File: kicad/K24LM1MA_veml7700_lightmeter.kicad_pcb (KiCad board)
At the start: 2 copper layers, 38.7 x 43.9 mm, 47 parts, among them J1 Conn_01x08_Socket, J2 Conn_01x08_Socket, J3 Conn_01x04_Socket, J4 Conn_01x04_Socket, J5 USB_C_Receptacle_USB2.0 USB41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, Q1 DMG3402L, Q2 DMG3402L, SW1 SW_Push, SW2 SW_Push, SW3 SW_Push, SW4 SW_Push, SW5 SW_Push, SW6 SW_SPST, U1 TP4056, U2 DW01A, U3 TPS73601DBV

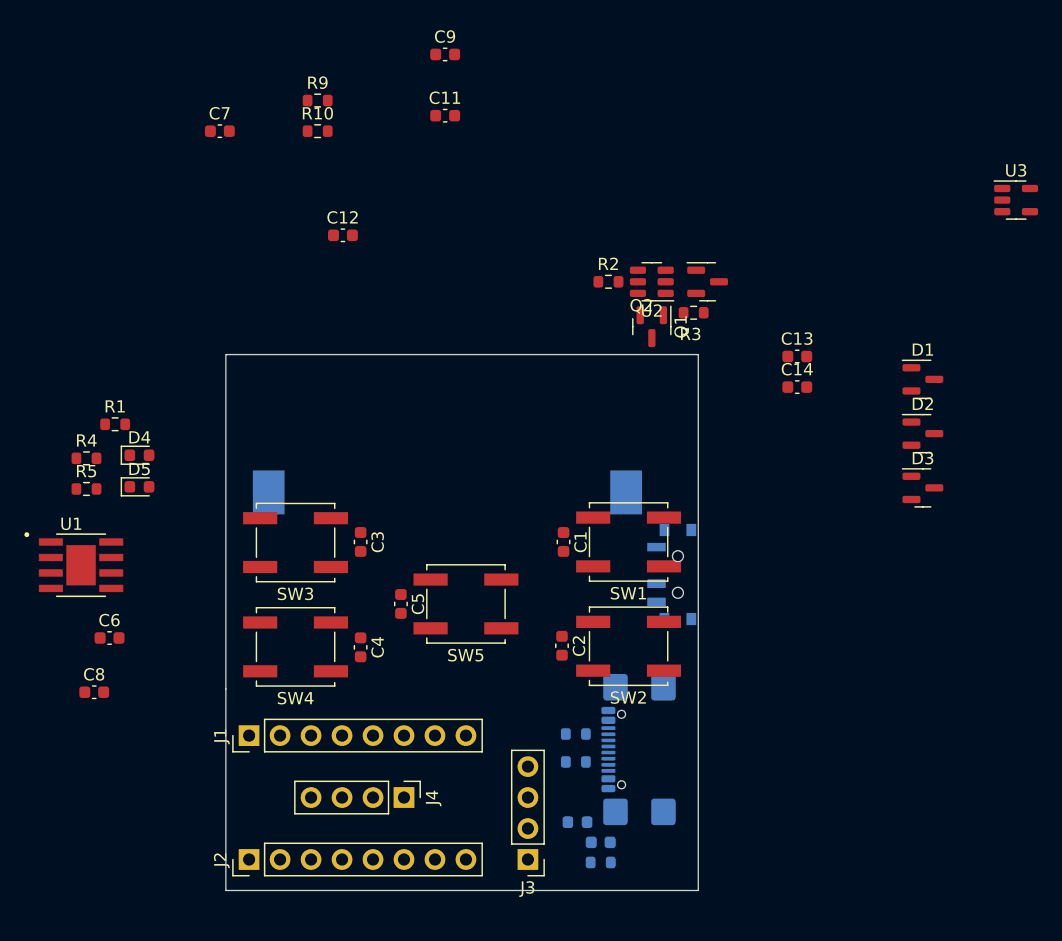
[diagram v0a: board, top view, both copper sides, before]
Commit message: finished layout, generated gerber files
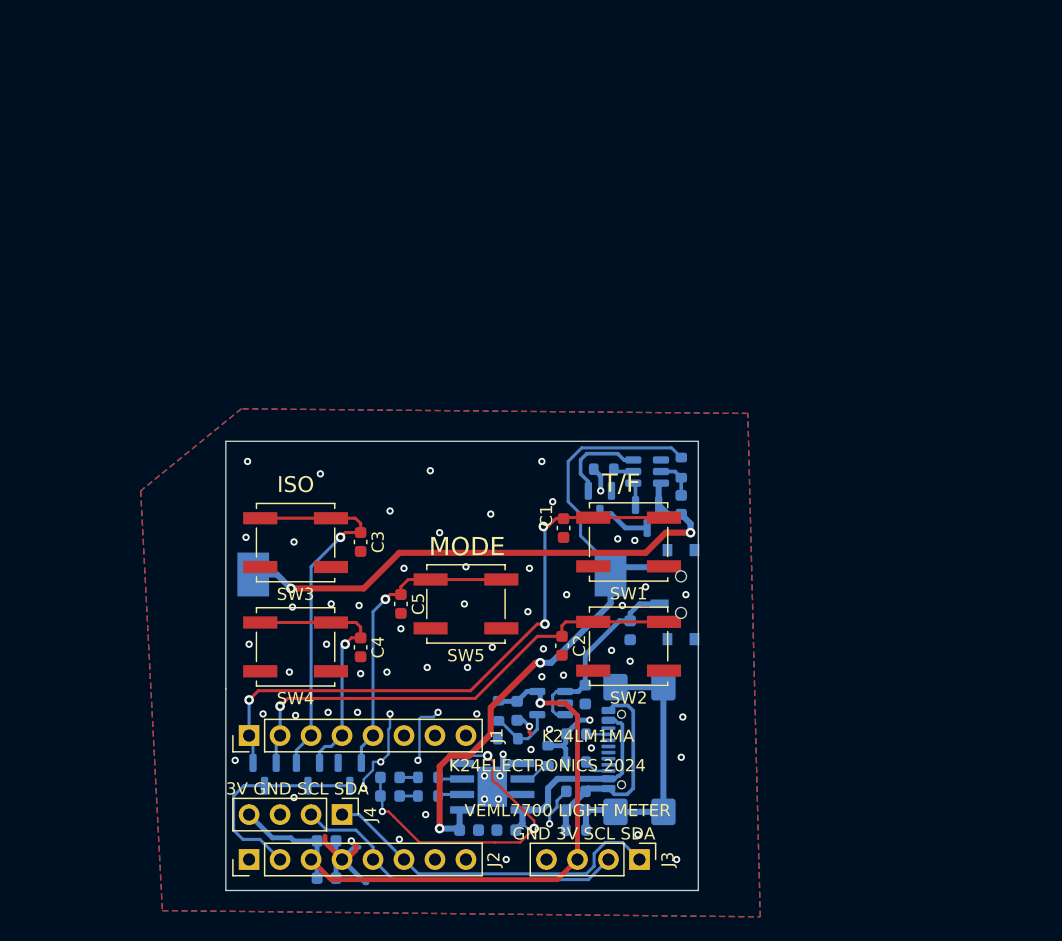
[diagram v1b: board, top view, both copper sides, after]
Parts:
- C11, C12, C13, C14, C6, C7, C8, C9, D1, D2, D3, D4, D5, Q1, Q2, R1, R10, R2, R3, R4, R5, R9, U1, U2, U3: moved to B.Cu
- moved D1 62.9 mm to (123.2, 130.2), turned to -90 degrees
- moved D2 57.6 mm to (126.7, 130.2), turned to -90 degrees
- moved U3 56.2 mm to (146.7, 124.3), turned to 180 degrees
- moved C14 55.8 mm to (128.3, 138.7), turned to 180 degrees
- moved C13 55.4 mm to (128.3, 135.6), turned to 180 degrees
- moved C7 53.0 mm to (153.2, 118.4), turned to 90 degrees
- moved D3 52.5 mm to (130.2, 130.2), turned to -90 degrees
- moved R10 52.2 mm to (143.1, 127.3)
- moved R9 52.2 mm to (142.4, 125.0), turned to 90 degrees
- moved C11 48.8 mm to (149.5, 123.6), turned to 90 degrees
- moved R1 44.7 mm to (146.4, 128.7), turned to 90 degrees
- moved C9 41.7 mm to (157.3, 108.1), turned to 90 degrees
- moved C12 41.5 mm to (143.9, 125.0), turned to 90 degrees
- moved R4 38.3 mm to (136.6, 130.4), turned to 180 degrees
- moved U1 38.3 mm to (141.9, 131.2), turned to 180 degrees
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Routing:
- net +BATT: track 0.00 -> 56.7 mm, vias 0 -> 2
- net +3V0: track 0.00 -> 53.0 mm, vias 0 -> 1
- net S_TP: track 0.00 -> 50.4 mm, vias 0 -> 3
- net GND: track 0.00 -> 47.0 mm, vias 0 -> 70
- net +5V: track 0.00 -> 45.3 mm, vias 0 -> 3
- net GND1: track 0.00 -> 44.1 mm, vias 0 -> 2
- net S_TN: track 0.00 -> 39.6 mm, vias 0 -> 1
- net S_IP: track 0.00 -> 31.0 mm, vias 0 -> 1
- net SDA: track 0.00 -> 28.6 mm
- net SCL: track 0.00 -> 27.9 mm
- net S_M: track 0.00 -> 24.8 mm, vias 0 -> 1
- net Net-(J5-SHIELD): track 0.00 -> 22.3 mm
- net S_IN: track 0.00 -> 21.7 mm, vias 0 -> 1
- net INT: track 0.00 -> 17.5 mm
- net Net-(C10-Pad1): track 0.00 -> 17.3 mm
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- added copper zone on B.Cu, net GND
- added copper zone on F.Cu, net GND
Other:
- board size 38.7 x 43.9 mm -> 38.7 x 36.8 mm
- board text added: "3V GND SCL SDA"
- board text added: "GND 3V SCL SDA"
- board text added: "ISO"
- board text added: "K24ELECTRONICS 2024"
- board text added: "K24LM1MA"
- board text added: "MODE"
- board text added: "T/F"
- board text added: "VEML7700 LIGHT METER"
